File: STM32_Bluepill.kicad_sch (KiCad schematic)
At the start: 28 parts, among them J1 USB_B_Micro, J2 Conn_01x04_Male, J3 Conn_01x04_Male, J4 Conn_01x04_Male, U1 STM32F103C8T6, U2 AMS1117-3.3, Y1 16MHz

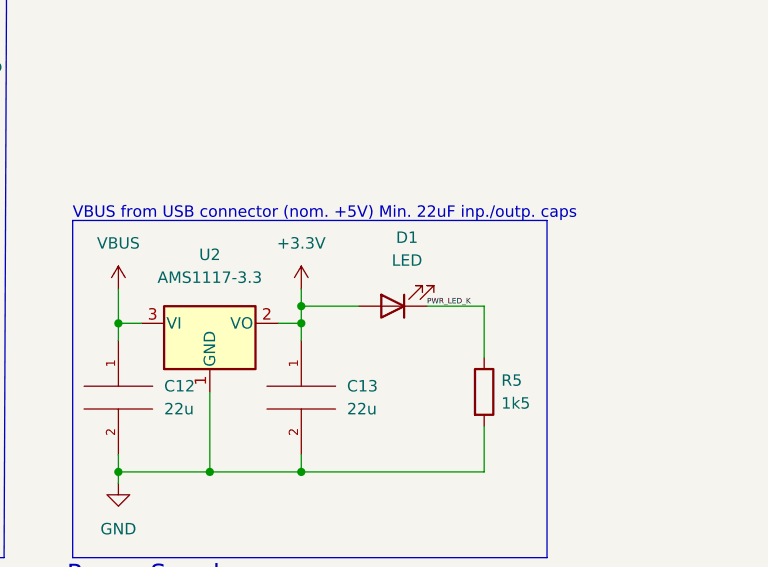
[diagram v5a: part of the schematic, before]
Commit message: Schematic: Change LED name to RED
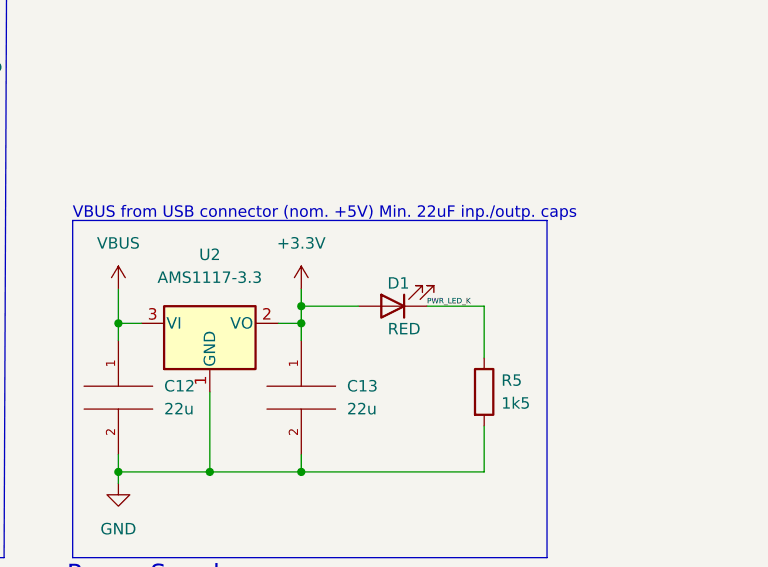
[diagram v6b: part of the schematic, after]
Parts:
- D1: value LED -> RED
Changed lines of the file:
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@@
   )
   (symbol (lib_id "Device:LED") (at 238.125 133.985 180) (unit 1)
-    (in_bom yes) (on_board yes) (fields_autoplaced)
-    (property "Reference" "D1" (id 0) (at 239.7125 126.365 0))
-    (property "Value" "LED" (id 1) (at 239.7125 128.905 0))
+    (in_bom yes) (on_board yes)
+    (property "Reference" "D1" (id 0) (at 238.76 131.445 0))
+    (property "Value" "RED" (id 1) (at 239.395 136.525 0))
     (property "Footprint" "" (id 2) (at 238.125 133.985 0)
       (effects (font (size 1.27 1.27)) hide)
@@
     )
     (path "/fa2f15a9-5e95-4684-b4d4-03d2c4578c27"
-      (reference "D1") (unit 1) (value "LED") (footprint "")
+      (reference "D1") (unit 1) (value "RED") (footprint "")
     )
     (path "/7ac34793-115a-4c6f-a05a-ce162dc72db3"

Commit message: Schematic: Assign footprints to schematic symbols
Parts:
- D1: footprint (none) -> LED_SMD:LED_0603_1608Metric
- FB1: footprint (none) -> Inductor_SMD:L_0603_1608Metric
- J1: footprint (none) -> Connector_USB:USB_Micro-B_Wuerth_629105150521
- J2, J3, J4: footprint (none) -> Connector_PinHeader_2.54mm:PinHeader_1x04_P2.54mm_Vertical
- R1, R2, R3, R4, R5: footprint (none) -> Resistor_SMD:R_0402_1005Metric
- SW_BOOT1: footprint (none) -> Button_Switch_THT:SW_E-Switch_EG1224_SPDT_Angled
- Y1: footprint (none) -> Crystal:Crystal_SMD_3225-4Pin_3.2x2.5mm
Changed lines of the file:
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@@
     (property "Reference" "J3" (id 0) (at 170.815 118.745 0))
     (property "Value" "Conn_01x04_Male" (id 1) (at 177.165 130.175 0))
-    (property "Footprint" "" (id 2) (at 170.815 123.825 0)
+    (property "Footprint" "Connector_PinHeader_2.54mm:PinHeader_1x04_P2.54mm_Vertical" (id 2) (at 170.815 123.825 0)
       (effects (font (size 1.27 1.27)) hide)
     )
@@
       (effects (font (size 1.27 1.27)) (justify left))
     )
-    (property "Footprint" "" (id 2) (at 246.507 143.51 90)
+    (property "Footprint" "Resistor_SMD:R_0402_1005Metric" (id 2) (at 246.507 143.51 90)
       (effects (font (size 1.27 1.27)) hide)
     )
@@
     (property "Reference" "R1" (id 0) (at 90.805 47.625 90))
     (property "Value" "10k" (id 1) (at 90.805 52.705 90))
-    (property "Footprint" "" (id 2) (at 90.805 51.943 90)
+    (property "Footprint" "Resistor_SMD:R_0402_1005Metric" (id 2) (at 90.805 51.943 90)
       (effects (font (size 1.27 1.27)) hide)
     )
@@
     (property "Reference" "FB1" (id 0) (at 178.3842 17.145 90))
     (property "Value" "120R" (id 1) (at 178.3842 19.685 90))
-    (property "Footprint" "" (id 2) (at 178.435 26.543 90)
+    (property "Footprint" "Inductor_SMD:L_0603_1608Metric" (id 2) (at 178.435 26.543 90)
       (effects (font (size 1.27 1.27)) hide)
     )
@@
       (effects (font (size 1.27 1.27)) (justify left))
     )
-    (property "Footprint" "" (id 2) (at 156.337 94.615 90)
+    (property "Footprint" "Resistor_SMD:R_0402_1005Metric" (id 2) (at 156.337 94.615 90)
       (effects (font (size 1.27 1.27)) hide)
     )
@@
     (property "Reference" "Y1" (id 0) (at 51.435 70.485 0))
     (property "Value" "16MHz" (id 1) (at 55.245 78.105 0))
-    (property "Footprint" "" (id 2) (at 48.895 75.565 0)
+    (property "Footprint" "Crystal:Crystal_SMD_3225-4Pin_3.2x2.5mm" (id 2) (at 48.895 75.565 0)
       (effects (font (size 1.27 1.27)) hide)
     )
@@
       (effects (font (size 1.27 1.27)) (justify right))
     )
-    (property "Footprint" "" (id 2) (at 175.895 99.695 0)
+    (property "Footprint" "Connector_USB:USB_Micro-B_Wuerth_629105150521" (id 2) (at 175.895 99.695 0)
       (effects (font (size 1.27 1.27)) hide)
     )
@@
     (property "Reference" "J4" (id 0) (at 36.83 139.065 0))
     (property "Value" "Conn_01x04_Male" (id 1) (at 27.94 149.225 0))
-    (property "Footprint" "" (id 2) (at 36.83 144.145 0)
+    (property "Footprint" "Connector_PinHeader_2.54mm:PinHeader_1x04_P2.54mm_Vertical" (id 2) (at 36.83 144.145 0)
       (effects (font (size 1.27 1.27)) hide)
     )
@@
       (effects (font (size 1.27 1.27)) (justify left))
     )
-    (property "Footprint" "" (id 2) (at 52.197 135.89 90)
+    (property "Footprint" "Resistor_SMD:R_0402_1005Metric" (id 2) (at 52.197 135.89 90)
       (effects (font (size 1.27 1.27)) hide)
     )
@@
       (effects (font (size 1.27 1.27)) (justify left))
     )
-    (property "Footprint" "" (id 2) (at 62.992 135.89 90)
+    (property "Footprint" "Resistor_SMD:R_0402_1005Metric" (id 2) (at 62.992 135.89 90)
       (effects (font (size 1.27 1.27)) hide)
     )
@@
     )
     (property "Value" "SW_SPDT" (id 1) (at 80.645 53.975 0))
-    (property "Footprint" "" (id 2) (at 76.835 50.165 0)
+    (property "Footprint" "Button_Switch_THT:SW_E-Switch_EG1224_SPDT_Angled" (id 2) (at 76.835 50.165 0)
       (effects (font (size 1.27 1.27)) hide)
     )
@@
     (property "Reference" "J2" (id 0) (at 36.83 113.03 0))
     (property "Value" "Conn_01x04_Male" (id 1) (at 27.94 123.19 0))
-    (property "Footprint" "" (id 2) (at 36.83 118.11 0)
+    (property "Footprint" "Connector_PinHeader_2.54mm:PinHeader_1x04_P2.54mm_Vertical" (id 2) (at 36.83 118.11 0)
       (effects (font (size 1.27 1.27)) hide)
     )
@@
     (property "Reference" "D1" (id 0) (at 238.76 131.445 0))
     (property "Value" "RED" (id 1) (at 239.395 136.525 0))
-    (property "Footprint" "" (id 2) (at 238.125 133.985 0)
+    (property "Footprint" "LED_SMD:LED_0603_1608Metric" (id 2) (at 238.125 133.985 0)
       (effects (font (size 1.27 1.27)) hide)
     )
@@
     )
     (path "/fa2f15a9-5e95-4684-b4d4-03d2c4578c27"
-      (reference "D1") (unit 1) (value "RED") (footprint "")
+      (reference "D1") (unit 1) (value "RED") (footprint "LED_SMD:LED_0603_1608Metric")
     )
     (path "/7ac34793-115a-4c6f-a05a-ce162dc72db3"
-      (reference "FB1") (unit 1) (value "120R") (footprint "")
+      (reference "FB1") (unit 1) (value "120R") (footprint "Inductor_SMD:L_0603_1608Metric")
     )
     (path "/9f1c510e-32d3-4302-89a0-0925ff949f4e"
-      (reference "J1") (unit 1) (value "USB_B_Micro") (footprint "")
+      (reference "J1") (unit 1) (value "USB_B_Micro") (footprint "Connector_USB:USB_Micro-B_Wuerth_629105150521")
     )
     (path "/f9621132-2ce6-4eae-9c94-8141158ef81c"
-      (reference "J2") (unit 1) (value "Conn_01x04_Male") (footprint "")
+      (reference "J2") (unit 1) (value "Conn_01x04_Male") (footprint "Connector_PinHeader_2.54mm:PinHeader_1x04_P2.54mm_Vertical")
     )
     (path "/17171bb8-0e09-4471-ab7d-f555055fe720"
-      (reference "J3") (unit 1) (value "Conn_01x04_Male") (footprint "")
+      (reference "J3") (unit 1) (value "Conn_01x04_Male") (footprint "Connector_PinHeader_2.54mm:PinHeader_1x04_P2.54mm_Vertical")
     )
     (path "/c5b0c5c9-8a87-4b70-a07f-2bb6f9c3381b"
-      (reference "J4") (unit 1) (value "Conn_01x04_Male") (footprint "")
+      (reference "J4") (unit 1) (value "Conn_01x04_Male") (footprint "Connector_PinHeader_2.54mm:PinHeader_1x04_P2.54mm_Vertical")
     )
     (path "/415aa6bb-21e9-4dd6-a1b4-c89c0b826bee"
-      (reference "R1") (unit 1) (value "10k") (footprint "")
+      (reference "R1") (unit 1) (value "10k") (footprint "Resistor_SMD:R_0402_1005Metric")
     )
     (path "/878c06a9-9fe0-4d98-8ca9-29ee5cfd6924"
-      (reference "R2") (unit 1) (value "1k5") (footprint "")
+      (reference "R2") (unit 1) (value "1k5") (footprint "Resistor_SMD:R_0402_1005Metric")
     )
     (path "/cdd9ee47-0188-4175-b3ac-e6b3a8007dfb"
-      (reference "R3") (unit 1) (value "1k5") (footprint "")
+      (reference "R3") (unit 1) (value "1k5") (footprint "Resistor_SMD:R_0402_1005Metric")
     )
     (path "/d4dd2e0c-c1af-46c1-b2ed-39c42fbee5fa"
-      (reference "R4") (unit 1) (value "1k5") (footprint "")
+      (reference "R4") (unit 1) (value "1k5") (footprint "Resistor_SMD:R_0402_1005Metric")
     )
     (path "/3b08fbf5-943f-4bc6-8a4e-9a8aab0eddc3"
-      (reference "R5") (unit 1) (value "1k5") (footprint "")
+      (reference "R5") (unit 1) (value "1k5") (footprint "Resistor_SMD:R_0402_1005Metric")
     )
     (path "/d5578dea-06c9-4c48-a263-f56a9b1bb322"
-      (reference "SW_BOOT1") (unit 1) (value "SW_SPDT") (footprint "")
+      (reference "SW_BOOT1") (unit 1) (value "SW_SPDT") (footprint "Button_Switch_THT:SW_E-Switch_EG1224_SPDT_Angled")
     )
     (path "/ffd66ea7-e38a-41a9-8818-d9efcb0dd031"
@@
     )
     (path "/8987f602-a9e1-4c91-a6b9-32bbf45b42c7"
-      (reference "Y1") (unit 1) (value "16MHz") (footprint "")
-    )
-  )
+      (reference "Y1") (unit 1) (value "16MHz") (footprint "Crystal:Crystal_SMD_3225-4Pin_3.2x2.5mm")
+    )
+  )
